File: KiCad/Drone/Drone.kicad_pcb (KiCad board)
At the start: 2 copper layers, 91.4 x 57.1 mm, 21 parts, among them J1 ESC, J10 to ESC Power, J2 BATTRY, J3 ESP32_LEFT, J4 Raspberry Pi, J5 ESP32_RIGHT, J6 DPS310_LEFT, J7 US-015, J8 MPU9250, J9 DPS310_RIGHT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

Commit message: [MOD]CS_PINの変更（回路の変更を含む）
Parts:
- moved J6 1.27 mm to (110.5, 96.5)
- moved J9 1.27 mm to (110.5, 109.2)
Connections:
- J3 pad 12: GPIO14 -> CSBN
- J3 pad 13: Echo -> GPIO12
- J3 pad 15: CSBN -> Echo
- J5 pad 8: GPIO19 -> ADO
- J5 pad 9: ADO -> GPIO18
- J6 pad 2: GPIO21 -> ADO
- J6 pad 3: ADO -> GPIO18
- J6 pad 4: GPIO19 -> GPIO23
- J7 pad 2: GPIO14 -> GPIO12
- J8 pad 3: GPIO21 -> GPIO18
- J8 pad 4: GPIO19 -> GPIO23
- U2 pad 1: GPIO23 -> GPIO21
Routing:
- net GPIO19: track 44.3 -> 0.00 mm
- net GPIO18: track 0.00 -> 38.9 mm
- net GND: track 165.1 -> 200.6 mm, vias 1 -> 6
- net GPIO23: track 24.9 -> 52.5 mm, vias 1 -> 0
- net 3V3: track 0.00 -> 24.3 mm, vias 0 -> 1
- net GPIO14: track 11.0 -> 0.00 mm
- net CSBN: track 7.18 -> 16.1 mm
- net GPIO12: track 0.00 -> 8.45 mm
- net Echo: track 11.0 -> 7.40 mm
- net GPIO17: track 31.3 -> 32.5 mm
- net GPIO15: track 25.2 -> 24.3 mm
- net GPIO4: track 26.0 -> 25.2 mm
- net GPIO21: track 35.1 -> 34.4 mm, vias 0 -> 1
- net ADO: track 27.8 -> 28.4 mm

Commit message: [MOD]外部5V電源とマイナーな変更
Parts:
- added J11: Conn_01x02_Female, Connector_PinHeader_2.54mm:PinHeader_1x02_P2.54mm_Vertical, F.Cu at (139.7, 121.9)
- moved C3 0.90 mm to (145.4, 117.5), turned to 180 degrees
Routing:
- net 5V: track 136.9 -> 189.7 mm
- net Net-(D2-Pad1): track 22.6 -> 20.7 mm
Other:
- board text added: "DRONE_PROJECT CIRCUIT_BOARD_V1"
- board text added: "Extra Power Delivery"
- board text added: "to ESC"
- board text added: "to LiPo"

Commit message: [MOD]minor change (#15)
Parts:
- moved J2 18.1 mm to (172.7, 119.7)
- moved J10 17.4 mm to (172.7, 101.6)
- moved C1 12.5 mm to (163.8, 107.2)
- moved D1 5.36 mm to (166.4, 106.8), turned to 90 degrees
- moved G*** 2.54 mm to (166.4, 83.8)
- moved U2 0.26 mm to (158.3, 100.3)
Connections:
- U2 pad 2: BAT -> ESC_VIN
- U2 pad 3: ESC_VIN -> BAT
- U2 pad 4: BAT -> ESC_VIN
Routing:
- net BAT: track 237.3 -> 102.6 mm, vias 15 -> 0
- net ESC_VIN: track 94.5 -> 169.5 mm, vias 0 -> 15
- net GND: track 200.6 -> 199.3 mm

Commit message: [MOD]シルクスクリーンのマイナーな変更 (#16)
* [MOD]minor change

* [MOD]minor change

* [MOD]UARTピンの変更
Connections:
- J5 pad 4: PI_PIGPIO_RX -> PI_UART_RX
- J5 pad 5: PI_PIGPIO_TX -> PI_UART_TX
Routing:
- net PI_UART_TX: track 0.00 -> 35.1 mm
- net PI_UART_RX: track 0.00 -> 35.0 mm
- net PI_PIGPIO_RX: track 25.0 -> 0.00 mm
- net PI_PIGPIO_TX: track 23.5 -> 0.00 mm

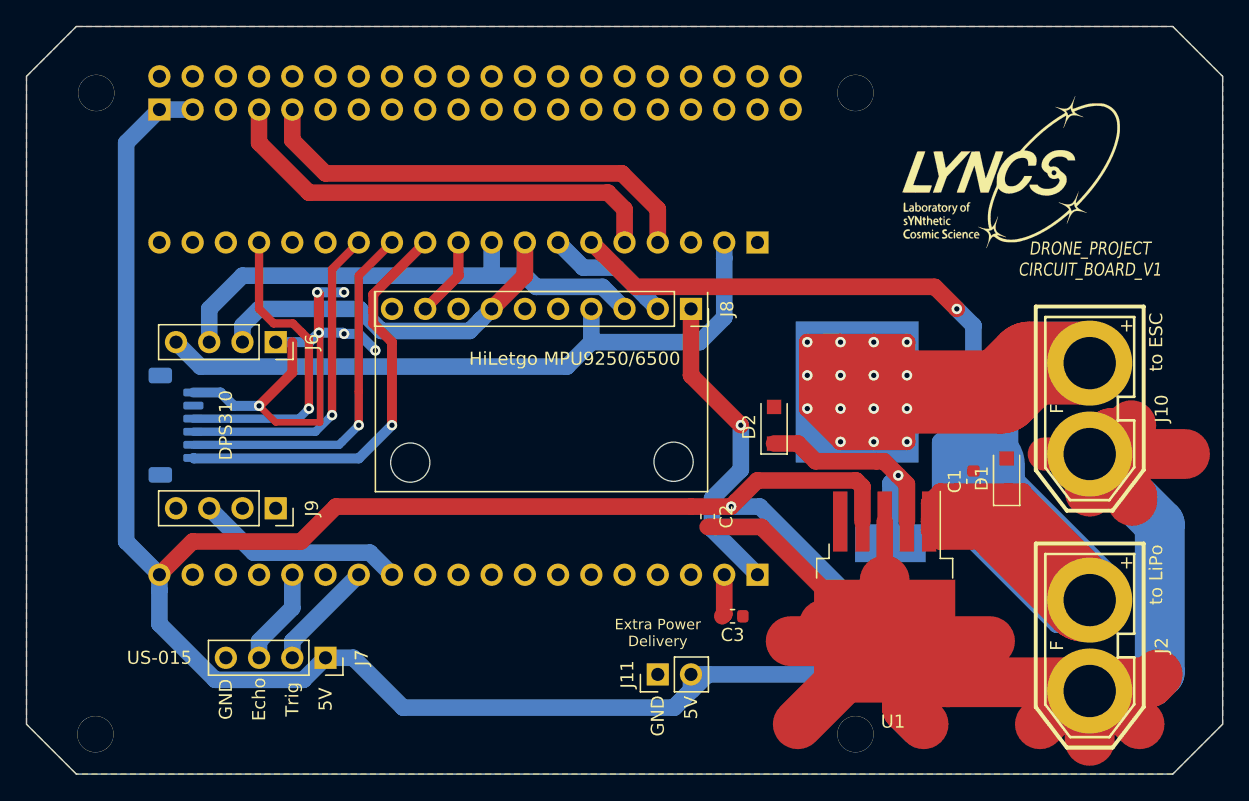
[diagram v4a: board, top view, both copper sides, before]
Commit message: [MOD]:recycle:回路の変更 (#21)
* [MOD]minor change

* [MOD]minor change

* [MOD]UARTピンの変更

* [MOD]:bug:MOSFET周りの修正

* :recycle:銅線を太くしたり
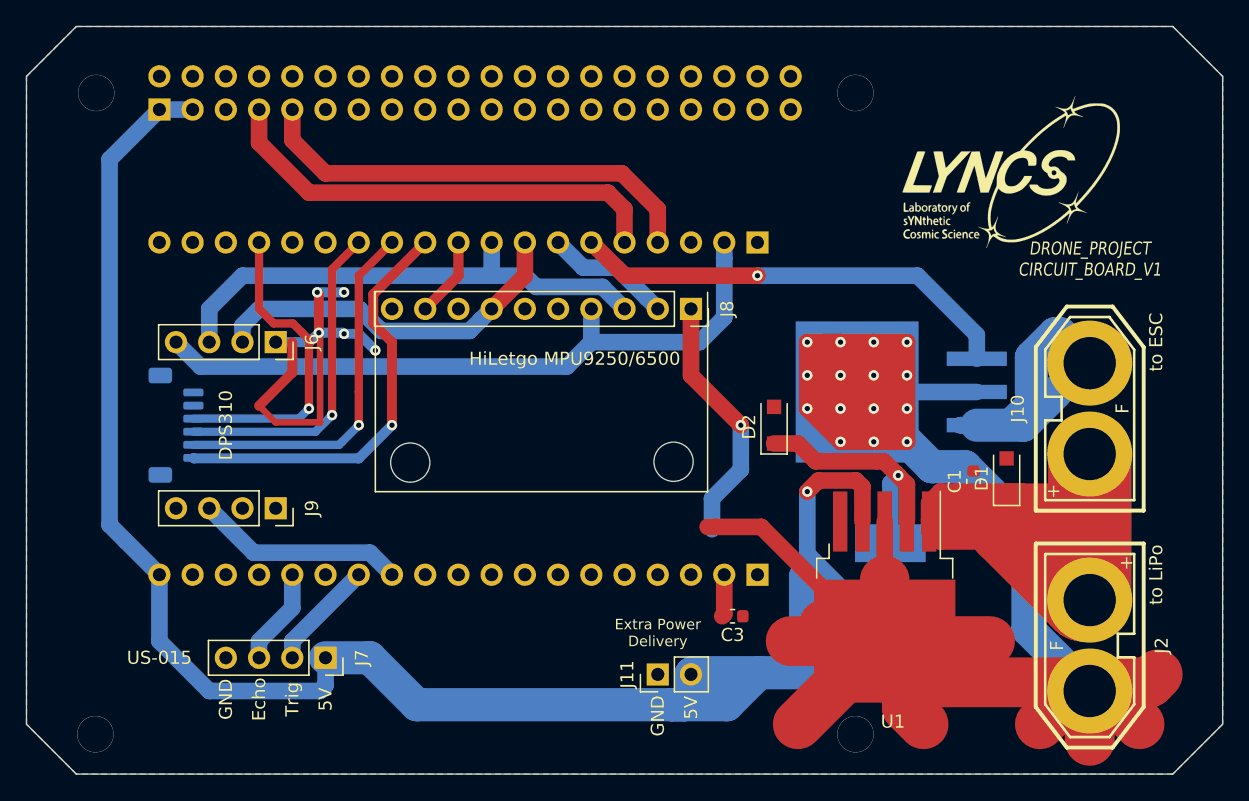
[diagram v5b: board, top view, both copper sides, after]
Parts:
- removed C2: 22u, Capacitor_SMD:C_0603_1608Metric
- turned J10 to 90 degrees
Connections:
- J1 pad 1: GND -> Net-(J1-Pad1)
- J10 pad 1: GND -> ESC_GND
- J10 pad 2: ESC_VIN -> BAT
- U2 pad 2: ESC_VIN -> GND
- U2 pad 3: BAT -> ESC_GND
- U2 pad 4: ESC_VIN -> GND
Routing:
- net ESC_VIN: track 169.5 -> 0.00 mm, vias 15 -> 0
- net GND: track 199.3 -> 307.8 mm, vias 6 -> 20
- net BAT: track 102.6 -> 73.1 mm
- net ESC_GND: track 0.00 -> 23.5 mm
- net 3V3: track 24.3 -> 19.3 mm
- net 5V: track 189.7 -> 193.9 mm
- net Net-(D2-Pad1): track 20.7 -> 19.7 mm

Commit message: :bug:ESCの位置と回路の変更
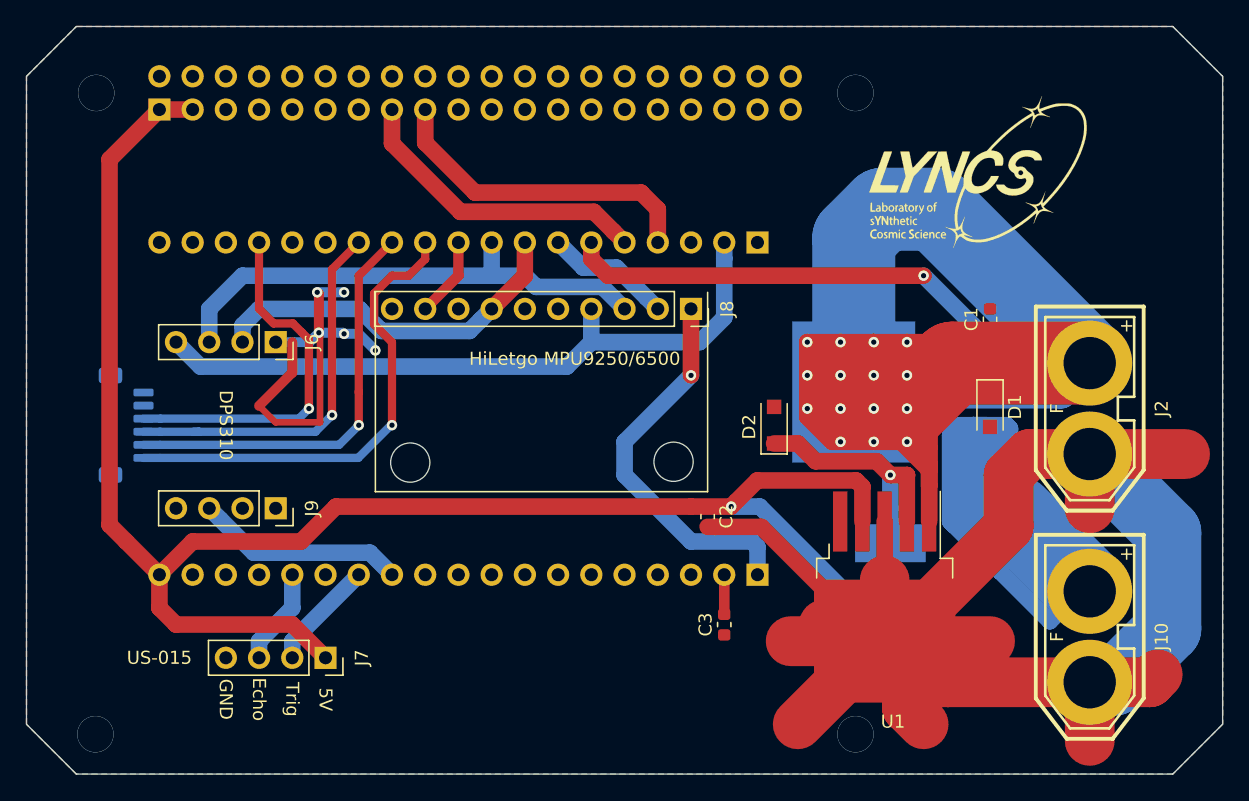
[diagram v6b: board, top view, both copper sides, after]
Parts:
- removed J11: Conn_01x02_Female, Connector_PinHeader_2.54mm:PinHeader_1x02_P2.54mm_Vertical
- added C2: 22u, Capacitor_SMD:C_0603_1608Metric, F.Cu at (143.5, 109.9)
- moved J2 18.1 mm to (172.7, 101.6)
- moved J10 17.4 mm to (172.7, 119.0), turned to 270 degrees
- moved C1 12.5 mm to (165.1, 94.8)
- moved D1 5.36 mm to (165.1, 101.6), turned to 270 degrees
- moved J1 3.81 mm to (99.1, 102.9)
- moved G*** 2.54 mm to (163.8, 83.8)
- moved C3 0.90 mm to (144.8, 118.1), turned to 90 degrees
- moved U2 0.26 mm to (158.1, 100.3)
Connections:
- J10 pad 1: ESC_GND -> GND
- J10 pad 2: BAT -> ESC_VIN
- J5 pad 4: PI_UART_RX -> PI_PIGPIO_RX
- J5 pad 5: PI_UART_TX -> PI_PIGPIO_TX
- U2 pad 2: GND -> BAT
- U2 pad 3: ESC_GND -> ESC_VIN
- U2 pad 4: GND -> BAT
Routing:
- net BAT: track 73.1 -> 256.6 mm, vias 0 -> 15
- net GND: track 307.8 -> 194.1 mm, vias 20 -> 5
- net ESC_VIN: track 0.00 -> 94.4 mm
- net 5V: track 193.9 -> 136.7 mm
- net PI_UART_TX: track 35.1 -> 0.00 mm
- net PI_UART_RX: track 35.0 -> 0.00 mm
- net PI_PIGPIO_RX: track 0.00 -> 25.0 mm
- net ESC_GND: track 23.5 -> 0.00 mm
- net PI_PIGPIO_TX: track 0.00 -> 23.5 mm
- net 3V3: track 19.3 -> 29.4 mm
- net GPIO17: track 32.5 -> 36.9 mm
- net GPIO4: track 25.2 -> 29.4 mm
- net GPIO16: track 28.3 -> 32.1 mm
- net GPIO15: track 24.3 -> 28.1 mm
- net Net-(D2-Pad1): track 19.7 -> 22.6 mm
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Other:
- board text removed: "DRONE_PROJECT CIRCUIT_BOARD_V1"
- board text removed: "Extra Power Delivery"
- board text removed: "to ESC"
- board text removed: "to LiPo"

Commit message: :recycle:微調整
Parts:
- removed C2: 22u, Capacitor_SMD:C_0603_1608Metric
- added J11: Conn_01x02_Female, Connector_PinHeader_2.54mm:PinHeader_1x02_P2.54mm_Vertical, F.Cu at (139.7, 121.9)
- moved J2 18.1 mm to (172.7, 119.7)
- moved J10 17.4 mm to (172.7, 101.6), turned to 90 degrees
- moved C1 12.5 mm to (163.8, 107.2)
- moved D1 5.36 mm to (166.4, 106.8), turned to 90 degrees
- moved J1 3.81 mm to (102.9, 102.9)
- moved J7 2.54 mm to (116.8, 120.7)
- moved G*** 2.54 mm to (166.4, 83.8)
- moved C3 0.90 mm to (145.4, 117.5), turned to 180 degrees
- moved U2 0.26 mm to (158.3, 100.3)
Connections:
- J10 pad 1: GND -> ESC_GND
- J10 pad 2: ESC_VIN -> BAT
- J5 pad 4: PI_PIGPIO_RX -> PI_UART_RX
- J5 pad 5: PI_PIGPIO_TX -> PI_UART_TX
- U2 pad 2: BAT -> GND
- U2 pad 3: ESC_VIN -> ESC_GND
- U2 pad 4: BAT -> GND
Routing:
- net BAT: track 256.6 -> 73.1 mm, vias 15 -> 0
- net GND: track 194.1 -> 368.0 mm, vias 5 -> 20
- net ESC_VIN: track 94.4 -> 0.00 mm
- net 5V: track 136.7 -> 202.0 mm
- net ESC_GND: track 0.00 -> 46.1 mm
- net PI_UART_TX: track 0.00 -> 35.1 mm
- net PI_UART_RX: track 0.00 -> 35.0 mm
- net PI_PIGPIO_RX: track 25.0 -> 0.00 mm
- net PI_PIGPIO_TX: track 23.5 -> 0.00 mm
- net 3V3: track 29.4 -> 19.3 mm
- net GPIO17: track 36.9 -> 32.5 mm
- net GPIO4: track 29.4 -> 25.2 mm
- net GPIO16: track 32.1 -> 28.3 mm
- net GPIO15: track 28.1 -> 24.3 mm
- net Net-(D2-Pad1): track 22.6 -> 19.7 mm
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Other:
- board text added: "DRONE_PROJECT CIRCUIT_BOARD_V1"
- board text added: "Extra Power Delivery"
- board text added: "to ESC"
- board text added: "to LiPo"
